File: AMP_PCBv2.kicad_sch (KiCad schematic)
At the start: 19 parts, among them U1 Teensy4.0, U2 Adafruit_Feather_M0_RFM9x_LoR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, U2 Logo

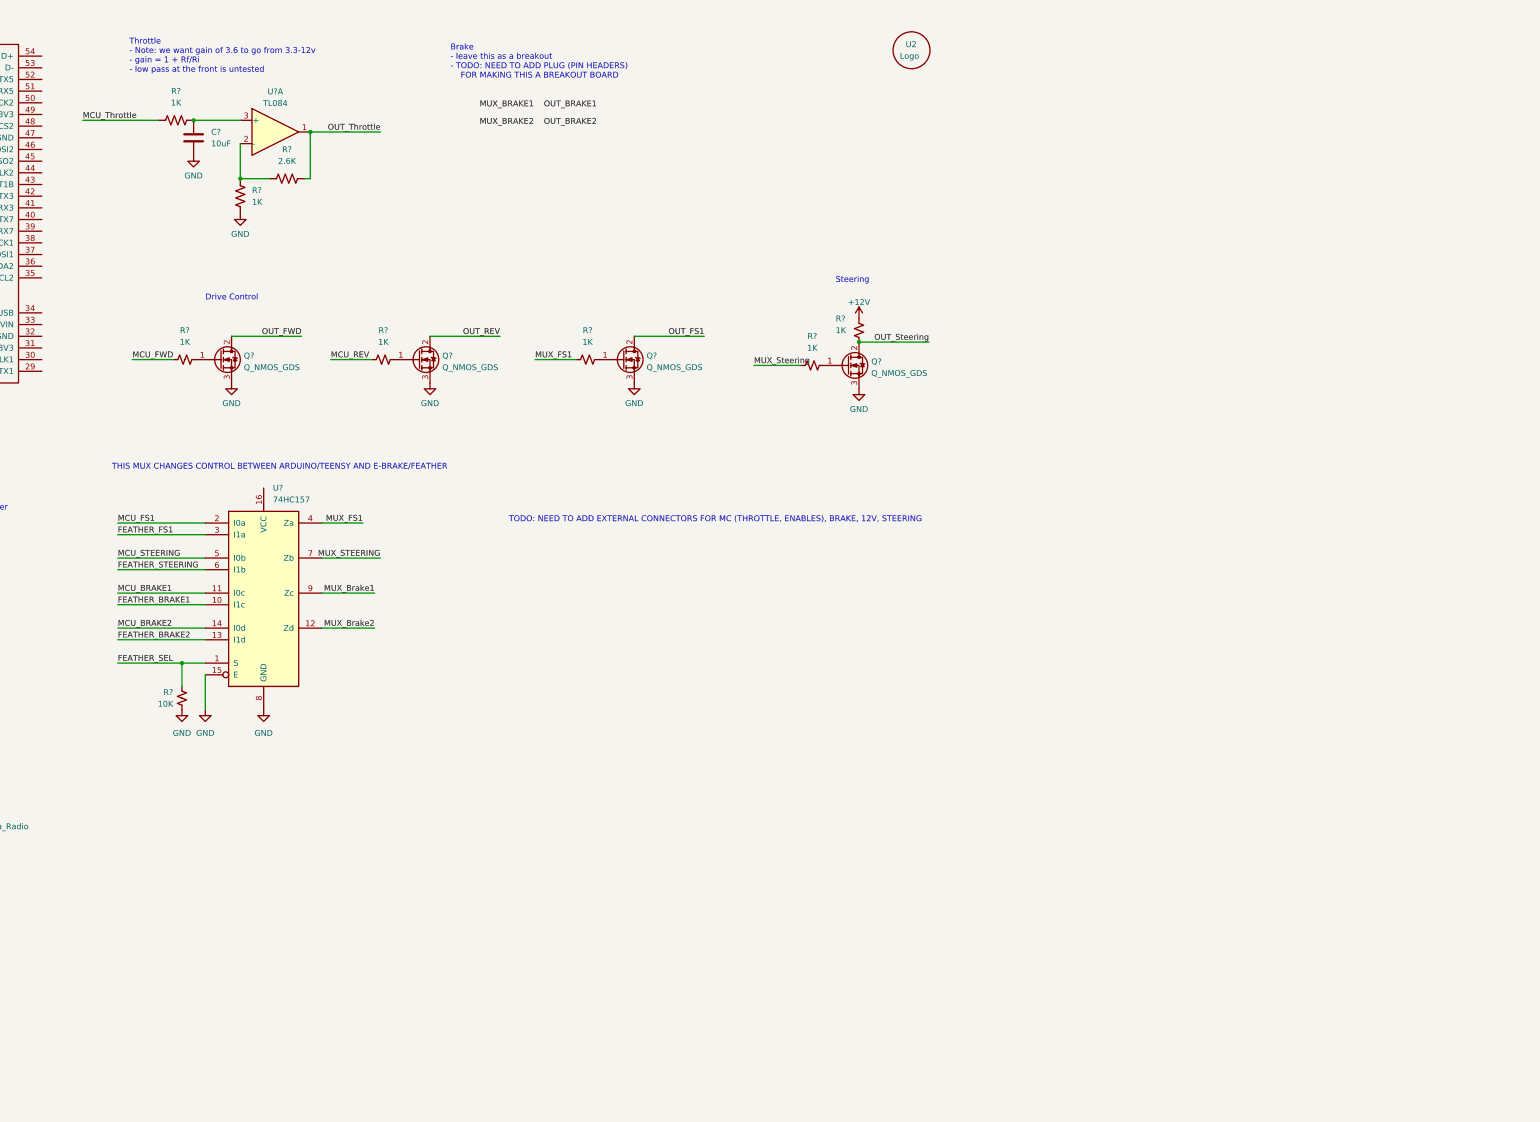
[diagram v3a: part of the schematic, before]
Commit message: Add mux chain, foot brake amplifier; schematic cleanup
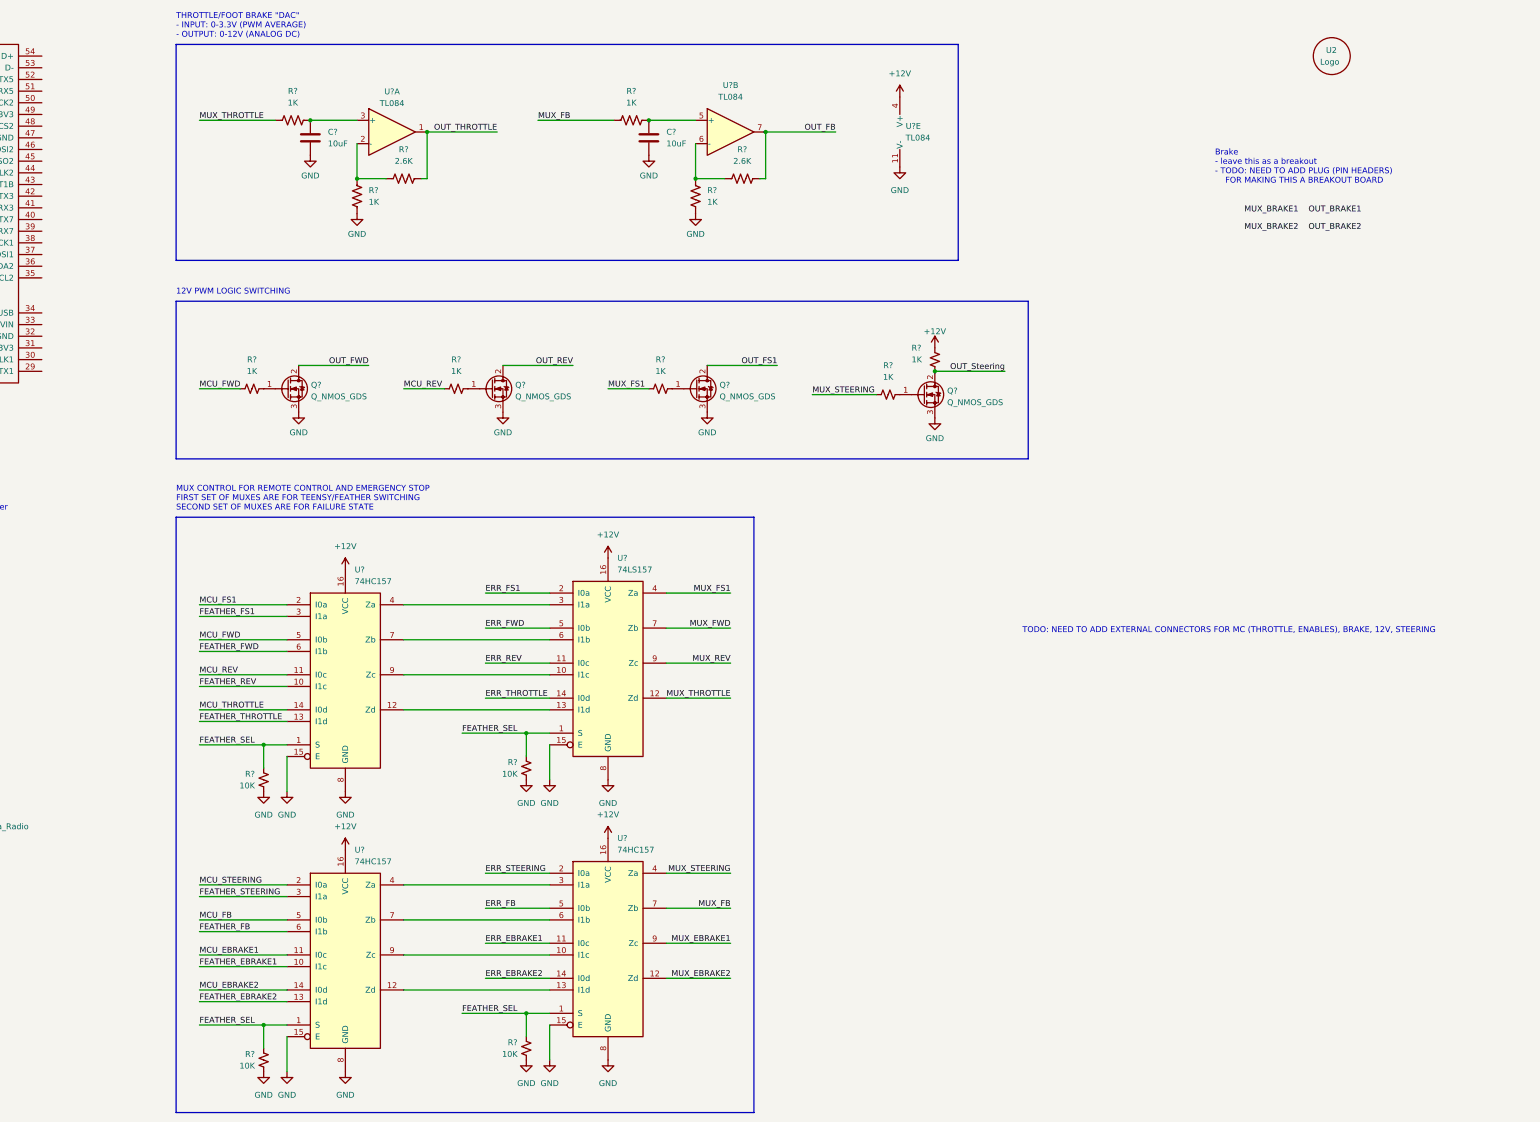
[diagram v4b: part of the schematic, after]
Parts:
- added C?: 10uF, symbol Device:C
- added R?: 2.6K, symbol Device:R_US
- added R? (x3): 10K, symbol Device:R_Small_US
- added R? (x2): 1K, symbol Device:R_US
- added U? (x2): TL084, symbol Amplifier_Operational:TL084
- added U? (x2): 74HC157, symbol 74xx:74LS157
- added U?: 74LS157, symbol 74xx:74LS157
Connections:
- net MCU_BRAKE1 is gone; now on net MCU_REV: U?.11 (I0c)
- net MUX_Steering is gone; now on net MUX_STEERING: R?.1
- net +12V: now also U?.16 (VCC), U?.16 (VCC), U?.16 (VCC), U?.16 (VCC), U?.4 (V+)
- net FEATHER_SEL: now also R?.1, R?.1, R?.1, U?.1 (S), U?.1 (S), U?.1 (S)
- net FEATHER_STEERING: now also U?.3 (I1a); no longer U?.6 (I1b)
- net GND: now also C?.2, R?.2, R?.2, R?.2, R?.2, U?.11 (V-), U?.15 (E), U?.15 (E), U?.15 (E), U?.8 (GND), U?.8 (GND), U?.8 (GND)
- net MCU_FWD: now also U?.5 (I0b)
- net MCU_STEERING: now also U?.2 (I0a); no longer U?.5 (I0b)
- net MUX_FS1: now also U?.4 (Za); no longer U?.4 (Za)
- net MUX_STEERING: now also U?.4 (Za); no longer U?.7 (Zb)
- net FEATHER_BRAKE1 renamed FEATHER_REV
- net FEATHER_BRAKE2 renamed FEATHER_THROTTLE
- net MCU_BRAKE2 renamed MCU_THROTTLE
- net MCU_Throttle renamed MUX_THROTTLE
- net MUX_THROTTLE: now also U?.12 (Zd)
- net MUX_Brake1: no longer names the net of U?.9 (Zc)
- net MUX_Brake1: now also U?.10 (I1c)
- net MUX_Brake2: no longer names the net of U?.12 (Zd)
- net MUX_Brake2: now also U?.13 (I1d)
- net OUT_Throttle renamed OUT_THROTTLE
- new net: R?.1, R?.1, U?.6 (-)
- new net: U?.10 (I1c), U?.9 (Zc)
- new net: U?.12 (Zd), U?.13 (I1d)
- new net: U?.3 (I1a), U?.4 (Za) (x2)
- new net: U?.6 (I1b), U?.7 (Zb) (x2)
- new net: C?.1, R?.2, U?.5 (+)
- new net ERR_EBRAKE1: U?.11 (I0c)
- new net ERR_EBRAKE2: U?.14 (I0d)
- new net ERR_FB: U?.5 (I0b)
- new net ERR_FS1: U?.2 (I0a)
- new net ERR_FWD: U?.5 (I0b)
- new net ERR_REV: U?.11 (I0c)
- new net ERR_STEERING: U?.2 (I0a)
- new net ERR_THROTTLE: U?.14 (I0d)
- new net FEATHER_EBRAKE1: U?.10 (I1c)
- new net FEATHER_EBRAKE2: U?.13 (I1d)
- new net FEATHER_FB: U?.6 (I1b)
- new net FEATHER_FWD: U?.6 (I1b)
- new net MCU_EBRAKE1: U?.11 (I0c)
- new net MCU_EBRAKE2: U?.14 (I0d)
- new net MCU_FB: U?.5 (I0b)
- new net MUX_EBRAKE1: U?.9 (Zc)
- new net MUX_EBRAKE2: U?.12 (Zd)
- new net MUX_FB: R?.1, U?.7 (Zb)
- new net MUX_FWD: U?.7 (Zb)
- new net MUX_REV: U?.9 (Zc)
- new net OUT_FB: R?.2, U?.7
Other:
- note added: "12V PWM LOGIC SWITCHING"
- note added: "MUX CONTROL FOR REMOTE CONTROL AND EMERGENCY STOP FIRST SET OF MUXES ARE FOR TEENSY/FEATHER SWITCHING SECOND SET OF MUXES ARE FOR FAILURE STATE"
- note added: "THROTTLE/FOOT BRAKE "DAC" - INPUT: 0-3.3V (PWM AVERAGE) - OUTPUT: 0-12V (ANALOG DC)"
- note removed: "Drive Control"
- note removed: "Steering"
- note removed: "THIS MUX CHANGES CONTROL BETWEEN ARDUINO/TEENSY AND E-BRAKE/FEATHER"
- note removed: "Throttle - Note: we want gain of 3.6 to go from 3.3-12v - gain = 1 + Rf/Ri - low pass at the front is untested"
- company: (none) -> Autonomous Motorsports Purdue
- title: (none) -> AMP PCBv2
- moved on the sheet: C?, Q?, R?, U2, U?, U?A

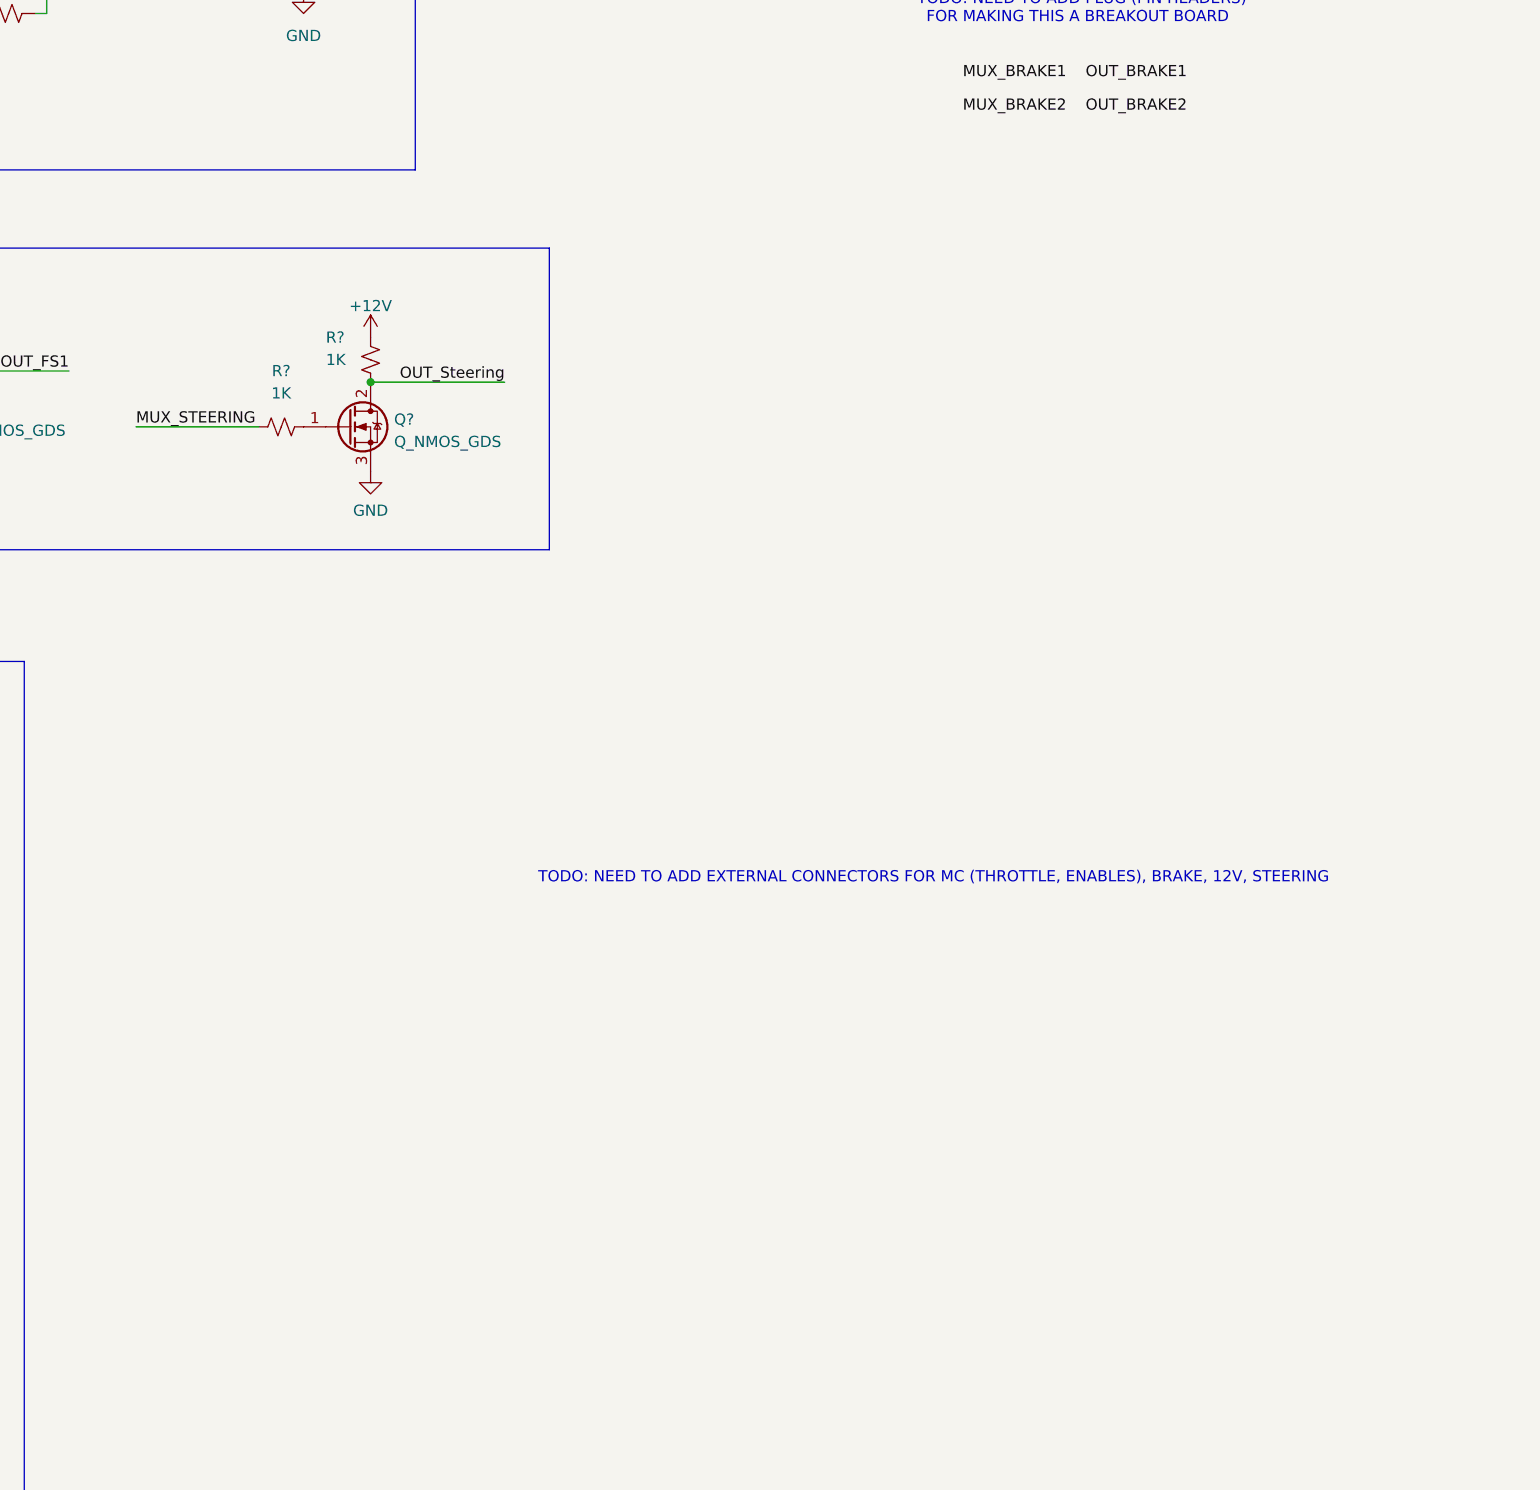
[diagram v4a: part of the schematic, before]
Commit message: Add wire-board connectors
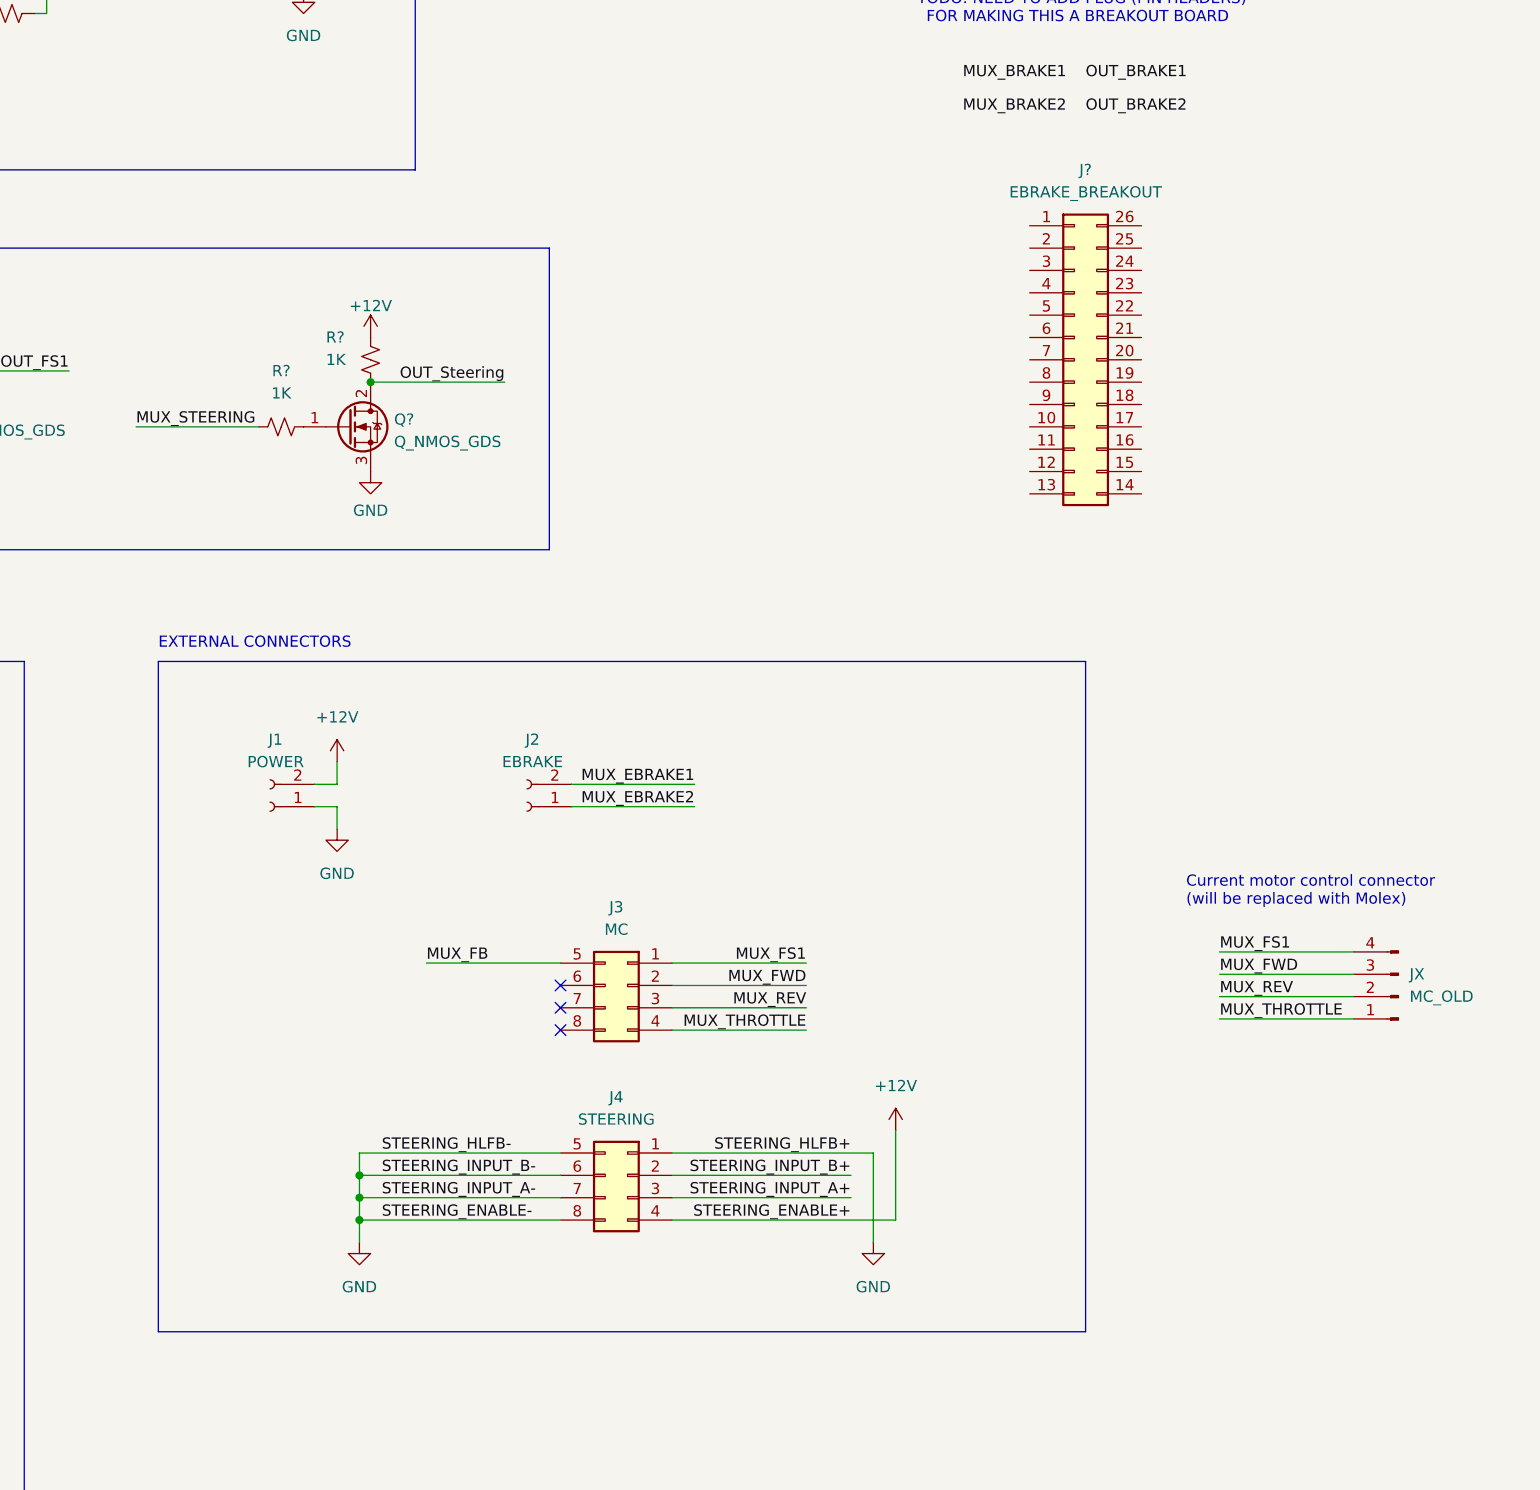
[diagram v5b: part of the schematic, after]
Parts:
- added J1: POWER, symbol Connector:Conn_01x02_Female
- added J2: EBRAKE, symbol Connector:Conn_01x02_Female
- added J3: MC, symbol Connector_Generic:Conn_02x04_Top_Bottom
- added J4: STEERING, symbol Connector_Generic:Conn_02x04_Top_Bottom
- added J?: EBRAKE_BREAKOUT, symbol Connector_Generic:Conn_02x13_Counter_Clockwise
- added JX: MC_OLD, symbol Connector:Conn_01x04_Male
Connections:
- net +12V: now also J1.2 (Pin_2), J4.4 (Pin_4)
- net GND: now also J1.1 (Pin_1), J4.1 (Pin_1), J4.5 (Pin_5), J4.6 (Pin_6), J4.7 (Pin_7), J4.8 (Pin_8)
- net MUX_EBRAKE1: now also J2.2 (Pin_2)
- net MUX_EBRAKE2: now also J2.1 (Pin_1)
- net MUX_FB: now also J3.5 (Pin_5)
- net MUX_FS1: now also J3.1 (Pin_1), JX.4 (Pin_4)
- net MUX_FWD: now also J3.2 (Pin_2), JX.3 (Pin_3)
- net MUX_REV: now also J3.3 (Pin_3), JX.2 (Pin_2)
- net MUX_THROTTLE: now also J3.4 (Pin_4), JX.1 (Pin_1)
- new net STEERING_INPUT_A+: J4.3 (Pin_3)
- new net STEERING_INPUT_B+: J4.2 (Pin_2)
- no-connect marks 0 -> 3
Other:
- note added: "Current motor control connector (will be replaced with Molex)"
- note added: "EXTERNAL CONNECTORS"
- note removed: "TODO: NEED TO ADD EXTERNAL CONNECTORS FOR MC (THROTTLE, ENABLES), BRAKE, 12V, STEERING"
